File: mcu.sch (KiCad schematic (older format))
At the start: 24 parts, among them SW1 PTS645VL39-2, U4 CAT24C32, U5 STM32F765VIT6, X1 ECS-TXO-3225-160-TR

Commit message: Current snapshot
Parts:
- removed C16: 4.7uF, Capacitor_SMD:C_0603_1608Metric, symbol Device:C
- R7, R8: value 47k -> 4.7k
- renumbered C17 to C16, C22 to C17, C25 to C22, C26 to C25, C28 to C26, C30 to C28, FB1 to FB2, FB2 to FB3
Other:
- moved on the sheet: C16, C17, C22, C25, C26, C28
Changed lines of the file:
@@
 $Descr A4 11693 8268
 encoding utf-8
-Sheet 4 7
+Sheet 4 11
 Title "MCU"
 Date ""
@@
 $Comp
 L Device:C C16
-U 1 1 5AD093F4
-P 1200 7300
-F 0 "C16" H 1315 7346 50  0000 L CNN
-F 1 "4.7uF" H 1315 7255 50  0000 L CNN
-F 2 "Capacitor_SMD:C_0603_1608Metric" H 1238 7150 50  0001 C CNN
-F 3 "~" H 1200 7300 50  0001 C CNN
-	1    1200 7300
+U 1 1 5AD0945E
+P 1150 7300
+F 0 "C16" H 1265 7346 50  0000 L CNN
+F 1 "100nF" H 1265 7255 50  0000 L CNN
+F 2 "Capacitor_SMD:C_0603_1608Metric" H 1188 7150 50  0001 C CNN
+F 3 "~" H 1150 7300 50  0001 C CNN
+	1    1150 7300
 	1    0    0    -1
 $EndComp
 $Comp
 L Device:C C17
-U 1 1 5AD0945E
-P 1650 7300
-F 0 "C17" H 1765 7346 50  0000 L CNN
-F 1 "100nF" H 1765 7255 50  0000 L CNN
-F 2 "Capacitor_SMD:C_0603_1608Metric" H 1688 7150 50  0001 C CNN
-F 3 "~" H 1650 7300 50  0001 C CNN
-	1    1650 7300
+U 1 1 5AD09C8C
+P 1600 7300
+F 0 "C17" H 1715 7346 50  0000 L CNN
+F 1 "100nF" H 1715 7255 50  0000 L CNN
+F 2 "Capacitor_SMD:C_0603_1608Metric" H 1638 7150 50  0001 C CNN
+F 3 "~" H 1600 7300 50  0001 C CNN
+	1    1600 7300
 	1    0    0    -1
 $EndComp
 $Comp
 L Device:C C22
-U 1 1 5AD09C8C
-P 2100 7300
-F 0 "C22" H 2215 7346 50  0000 L CNN
-F 1 "100nF" H 2215 7255 50  0000 L CNN
-F 2 "Capacitor_SMD:C_0603_1608Metric" H 2138 7150 50  0001 C CNN
-F 3 "~" H 2100 7300 50  0001 C CNN
-	1    2100 7300
+U 1 1 5AD09D94
+P 2050 7300
+F 0 "C22" H 2165 7346 50  0000 L CNN
+F 1 "100nF" H 2165 7255 50  0000 L CNN
+F 2 "Capacitor_SMD:C_0603_1608Metric" H 2088 7150 50  0001 C CNN
+F 3 "~" H 2050 7300 50  0001 C CNN
+	1    2050 7300
 	1    0    0    -1
 $EndComp
 $Comp
 L Device:C C25
-U 1 1 5AD09D94
-P 2550 7300
-F 0 "C25" H 2665 7346 50  0000 L CNN
-F 1 "100nF" H 2665 7255 50  0000 L CNN
-F 2 "Capacitor_SMD:C_0603_1608Metric" H 2588 7150 50  0001 C CNN
-F 3 "~" H 2550 7300 50  0001 C CNN
-	1    2550 7300
+U 1 1 5AD09D9B
+P 2500 7300
+F 0 "C25" H 2615 7346 50  0000 L CNN
+F 1 "100nF" H 2615 7255 50  0000 L CNN
+F 2 "Capacitor_SMD:C_0603_1608Metric" H 2538 7150 50  0001 C CNN
+F 3 "~" H 2500 7300 50  0001 C CNN
+	1    2500 7300
 	1    0    0    -1
 $EndComp
 $Comp
 L Device:C C26
-U 1 1 5AD09D9B
-P 3000 7300
-F 0 "C26" H 3115 7346 50  0000 L CNN
-F 1 "100nF" H 3115 7255 50  0000 L CNN
-F 2 "Capacitor_SMD:C_0603_1608Metric" H 3038 7150 50  0001 C CNN
-F 3 "~" H 3000 7300 50  0001 C CNN
-	1    3000 7300
-	1    0    0    -1
-$EndComp
-$Comp
-L Device:C C28
 U 1 1 5AD09E94
-P 3450 7300
-F 0 "C28" H 3565 7346 50  0000 L CNN
-F 1 "100nF" H 3565 7255 50  0000 L CNN
-F 2 "Capacitor_SMD:C_0603_1608Metric" H 3488 7150 50  0001 C CNN
-F 3 "~" H 3450 7300 50  0001 C CNN
-	1    3450 7300
-	1    0    0    -1
-$EndComp
-Wire Wire Line
-	950  7150 1200 7150
-Connection ~ 1200 7150
-Wire Wire Line
-	1200 7150 1650 7150
-Connection ~ 1650 7150
-Wire Wire Line
-	1650 7150 2100 7150
-Connection ~ 2100 7150
-Wire Wire Line
-	2100 7150 2550 7150
-Connection ~ 2550 7150
-Wire Wire Line
-	2550 7150 3000 7150
-Connection ~ 3000 7150
-Wire Wire Line
-	3000 7150 3450 7150
-Connection ~ 1200 7450
-Wire Wire Line
-	1200 7450 950  7450
-Connection ~ 1650 7450
-Wire Wire Line
-	1650 7450 1200 7450
-Connection ~ 2100 7450
-Wire Wire Line
-	2100 7450 1650 7450
-Connection ~ 2550 7450
-Wire Wire Line
-	2550 7450 2100 7450
-Connection ~ 3000 7450
-Wire Wire Line
-	3000 7450 2550 7450
-Wire Wire Line
-	3450 7450 3000 7450
+P 2950 7300
+F 0 "C26" H 3065 7346 50  0000 L CNN
+F 1 "100nF" H 3065 7255 50  0000 L CNN
+F 2 "Capacitor_SMD:C_0603_1608Metric" H 2988 7150 50  0001 C CNN
+F 3 "~" H 2950 7300 50  0001 C CNN
+	1    2950 7300
+	1    0    0    -1
+$EndComp
 Text Notes 1650 7550 0    50   ~ 0
 Place as close as possible to pins!
@@
 $EndComp
 $Comp
-L Device:Ferrite_Bead_Small FB1
+L Device:Ferrite_Bead_Small FB2
 U 1 1 5AF6D789
 P 1250 6400
-F 0 "FB1" V 1013 6400 50  0000 C CNN
+F 0 "FB2" V 1013 6400 50  0000 C CNN
 F 1 "MPZ1608S221A" V 1104 6400 50  0000 C CNN
 F 2 "Resistor_SMD:R_0603_1608Metric" V 1180 6400 50  0001 C CNN
@@
 $EndComp
 $Comp
-L Device:Ferrite_Bead_Small FB2
+L Device:Ferrite_Bead_Small FB3
 U 1 1 5AF6DF9B
 P 1350 6500
-F 0 "FB2" V 1500 6450 50  0000 C CNN
+F 0 "FB3" V 1500 6450 50  0000 C CNN
 F 1 "MPZ1608S221A" V 1600 6450 50  0000 C CNN
 F 2 "Resistor_SMD:R_0603_1608Metric" V 1280 6500 50  0001 C CNN
@@
 VDD3V3
 $Comp
-L Device:C C30
+L Device:C C28
 U 1 1 5BC224AB
-P 3900 7300
-F 0 "C30" H 4015 7346 50  0000 L CNN
-F 1 "100nF" H 4015 7255 50  0000 L CNN
-F 2 "Capacitor_SMD:C_0603_1608Metric" H 3938 7150 50  0001 C CNN
-F 3 "~" H 3900 7300 50  0001 C CNN
-	1    3900 7300
-	1    0    0    -1
-$EndComp
-Wire Wire Line
-	3450 7150 3900 7150
-Connection ~ 3450 7150
-Wire Wire Line
-	3450 7450 3900 7450
-Connection ~ 3450 7450
+P 3400 7300
+F 0 "C28" H 3515 7346 50  0000 L CNN
+F 1 "100nF" H 3515 7255 50  0000 L CNN
+F 2 "Capacitor_SMD:C_0603_1608Metric" H 3438 7150 50  0001 C CNN
+F 3 "~" H 3400 7300 50  0001 C CNN
+	1    3400 7300
+	1    0    0    -1
+$EndComp
 Wire Wire Line
 	1300 4350 1300 4550
@@
 P 9600 5950
 F 0 "R7" H 9400 5900 50  0000 L CNN
-F 1 "47k" H 9400 6000 50  0000 L CNN
+F 1 "4.7k" H 9400 6000 50  0000 L CNN
 F 2 "Resistor_SMD:R_0603_1608Metric" V 9530 5950 50  0001 C CNN
 F 3 "~" H 9600 5950 50  0001 C CNN
@@
 P 9900 5950
 F 0 "R8" H 9700 5900 50  0000 L CNN
-F 1 "47k" H 9700 6000 50  0000 L CNN
+F 1 "4.7k" H 9700 6000 50  0000 L CNN
 F 2 "Resistor_SMD:R_0603_1608Metric" V 9830 5950 50  0001 C CNN
 F 3 "~" H 9900 5950 50  0001 C CNN
@@
 Wire Wire Line
 	7850 5100 7850 4600
+Wire Wire Line
+	950  7150 1150 7150
+Wire Wire Line
+	950  7450 1150 7450
+Connection ~ 1150 7150
+Wire Wire Line
+	1150 7150 1600 7150
+Connection ~ 1150 7450
+Wire Wire Line
+	1150 7450 1600 7450
+Connection ~ 1600 7150
+Connection ~ 1600 7450
+Connection ~ 2050 7150
+Connection ~ 2050 7450
+Connection ~ 2500 7150
+Connection ~ 2500 7450
+Connection ~ 2950 7150
+Connection ~ 2950 7450
+Wire Wire Line
+	1600 7150 2050 7150
+Wire Wire Line
+	2050 7150 2500 7150
+Wire Wire Line
+	2500 7150 2950 7150
+Wire Wire Line
+	2950 7150 3400 7150
+Wire Wire Line
+	2050 7450 2500 7450
+Wire Wire Line
+	2500 7450 2950 7450
+Wire Wire Line
+	2950 7450 3400 7450
+Wire Wire Line
+	1600 7450 2050 7450
 $EndSCHEMATC

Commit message: First pass of routing
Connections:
- net SCL: now also U5.92 (PB6)
- net SDA: now also U5.96 (PB9)
- net Z_MIN: now reaches U5.1 (PE2)
- net TEMP4: now reaches U5.15 (PC0)
- net TEMP3: now reaches U5.16 (PC1)
- net TEMP2: now reaches U5.17 (PC2)
- net TEMP1: now reaches U5.18 (PC3)
- net Y_MIN: now reaches U5.2 (PE3)
- net PWM_HEAT1: now reaches U5.22 (PA0-WKUP)
- net STEP_Z: now reaches U5.23 (PA1)
- net STEP_Y: now reaches U5.24 (PA2)
- net STEP_X: now reaches U5.25 (PA3)
- net MCU_SS: now reaches U5.28 (PA4)
- net SPI1_SCK: now reaches U5.29 (PA5)
- net X_MIN: now reaches U5.3 (PE4)
- net SPI1_MISO: now reaches U5.30 (PA6)
- net SPI1_MOSI: now reaches U5.31 (PA7)
- net DIR_Z: now reaches U5.33 (PC5)
- net SS_Z: now reaches U5.34 (PB0)
- net DIR_Y: now reaches U5.35 (PB1)
- net SS_Y: now reaches U5.36 (PB2)
- net DIR_X: now reaches U5.37 (PE7)
- net SS_X: now reaches U5.38 (PE8)
- net PWM_BED: now reaches U5.4 (PE5)
- net SPI4_SCK: now reaches U5.42 (PE12)
- net SPI4_MISO: now reaches U5.43 (PE13)
- net SPI4_MOSI: now reaches U5.44 (PE14)
- net DIR_E1: now reaches U5.46 (PB10)
- net PWM_HEAT2: now reaches U5.5 (PE6)
- net SS_E1: now reaches U5.51 (PB12)
- net DIR_E0: now reaches U5.52 (PB13)
- net STEP_E1: now reaches U5.53 (PB14)
- net STEP_E0: now reaches U5.54 (PB15)
- net SS_E0: now reaches U5.56 (PD9)
- net SS_SD: now reaches U5.57 (PD10)
- net SD_DETECT: now reaches U5.58 (PD11)
- net PWM_FAN1: now reaches U5.59 (PD12)
- net PWM_FAN2: now reaches U5.60 (PD13)
- net PWM_FAN3: now reaches U5.61 (PD14)
- net PWM_FAN4: now reaches U5.62 (PD15)
- net PWM_EXT4: now reaches U5.63 (PC6)
- net PWM_EXT3: now reaches U5.64 (PC7)
- net PWM_EXT2: now reaches U5.65 (PC8)
- net PWM_EXT1: now reaches U5.66 (PC9)
- net USART1_TX: now reaches U5.68 (PA9)
- net USART1_RX: now reaches U5.69 (PA10)
- net SWDIO: now reaches U5.72 (PA13)
- net SWCLK: now reaches U5.76 (PA14)
- net USART3_TX: now reaches U5.78 (PC10)
- net USART3_RX: now reaches U5.79 (PC11)
- net D5: now reaches U5.83 (PD2)
- net D4: now reaches U5.84 (PD3)
- net D3: now reaches U5.85 (PD4)
- net D2: now reaches U5.86 (PD5)
- net D1: now reaches U5.87 (PD6)
- net SWO: now reaches U5.89 (PB3)
- no-connect marks 3 -> 25
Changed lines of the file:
@@
 	0    1    1    0
-$EndComp
-$Comp
-L heteromycin:STM32F765VIT6 U5
-U 1 1 5AD0AB9A
-P 6750 3000
-F 0 "U5" H 6750 3000 50  0000 L CNN
-F 1 "STM32F765VIT6" H 6500 2900 50  0000 L CNN
-F 2 "heteromycin:TQFP-100_14x14mm_P0.5mm" H 6750 3000 50  0001 C CNN
-F 3 "http://www.st.com/en/microcontrollers/stm32f765vi.html" H 6750 3000 50  0001 C CNN
-	1    6750 3000
-	1    0    0    -1
 $EndComp
 Text HLabel 10400 6200 2    50   Input ~ 0
@@
 Wire Wire Line
 	1600 7450 2050 7450
+Text HLabel 5150 2100 0    50   Input ~ 0
+PWM_BED
+Text HLabel 5150 2200 0    50   Input ~ 0
+PWM_HEAT2
+Text HLabel 5150 3500 0    50   Input ~ 0
+TEMP1
+Text HLabel 5150 3400 0    50   Input ~ 0
+TEMP2
+Text HLabel 5150 3300 0    50   Input ~ 0
+TEMP3
+Text HLabel 5150 3200 0    50   Input ~ 0
+TEMP4
+Text HLabel 5150 3900 0    50   Input ~ 0
+PWM_HEAT1
+Text HLabel 5150 4000 0    50   Input ~ 0
+STEP_Z
+Text HLabel 5150 4100 0    50   Input ~ 0
+STEP_Y
+Text HLabel 5150 4200 0    50   Input ~ 0
+STEP_X
+Text HLabel 5850 4600 3    50   Input ~ 0
+SPI1_SCK
+Text HLabel 5950 4600 3    50   Input ~ 0
+SPI1_MISO
+Text HLabel 6050 4600 3    50   Input ~ 0
+SPI1_MOSI
+NoConn ~ 6150 4600
+NoConn ~ 6850 4600
+NoConn ~ 6950 4600
+Text HLabel 6350 4600 3    50   Input ~ 0
+SS_Z
+Text HLabel 6250 4600 3    50   Input ~ 0
+DIR_Z
+Text HLabel 6550 4600 3    50   Input ~ 0
+SS_Y
+Text HLabel 6450 4600 3    50   Input ~ 0
+DIR_Y
+Text HLabel 6750 4600 3    50   Input ~ 0
+SS_X
+Text HLabel 5750 4600 3    50   Input ~ 0
+MCU_SS
+Text HLabel 7150 4600 3    50   Input ~ 0
+SPI4_SCK
+Text HLabel 7250 4600 3    50   Input ~ 0
+SPI4_MISO
+NoConn ~ 7450 4600
+Text HLabel 7350 4600 3    50   Input ~ 0
+SPI4_MOSI
+Text HLabel 7550 4600 3    50   Input ~ 0
+DIR_E1
+Text HLabel 8350 4200 2    50   Input ~ 0
+SS_E1
+Text HLabel 8350 4100 2    50   Input ~ 0
+DIR_E0
+Text HLabel 8350 3700 2    50   Input ~ 0
+SS_E0
+Text HLabel 8350 4000 2    50   Input ~ 0
+STEP_E1
+Text HLabel 8350 3900 2    50   Input ~ 0
+STEP_E0
+Text HLabel 8350 3400 2    50   Input ~ 0
+PWM_FAN1
+Text HLabel 8350 3300 2    50   Input ~ 0
+PWM_FAN2
+Text HLabel 8350 3200 2    50   Input ~ 0
+PWM_FAN3
+Text HLabel 8350 3100 2    50   Input ~ 0
+PWM_FAN4
+Text HLabel 8350 2700 2    50   Input ~ 0
+PWM_EXT1
+Text HLabel 8350 2800 2    50   Input ~ 0
+PWM_EXT2
+Text HLabel 8350 2900 2    50   Input ~ 0
+PWM_EXT3
+Text HLabel 8350 3000 2    50   Input ~ 0
+PWM_EXT4
+Text HLabel 8350 2500 2    50   Input ~ 0
+USART1_TX
+Text HLabel 8350 2400 2    50   Input ~ 0
+USART1_RX
+NoConn ~ 8350 2300
+Text HLabel 8350 3600 2    50   Input ~ 0
+SS_SD
+NoConn ~ 8350 2600
+NoConn ~ 8350 2200
+Text HLabel 8350 2100 2    50   Input ~ 0
+SWDIO
+Text HLabel 7950 1400 1    50   Input ~ 0
+SWCLK
+Text HLabel 6650 1400 1    50   Input ~ 0
+SWO
+Text HLabel 7750 1400 1    50   Input ~ 0
+USART3_TX
+Text HLabel 7650 1400 1    50   Input ~ 0
+USART3_RX
+Text HLabel 6350 1400 1    50   Input ~ 0
+SCL
+Text HLabel 5950 1400 1    50   Input ~ 0
+SDA
+NoConn ~ 5150 2400
+NoConn ~ 7850 1400
+NoConn ~ 7550 1400
+NoConn ~ 7450 1400
+NoConn ~ 6750 1400
+NoConn ~ 6550 1400
+NoConn ~ 6450 1400
+NoConn ~ 6250 1400
+NoConn ~ 6050 1400
+NoConn ~ 5850 1400
+NoConn ~ 5750 1400
+Text HLabel 6650 4600 3    50   Input ~ 0
+DIR_X
+NoConn ~ 8350 3800
+NoConn ~ 7650 4600
+Text HLabel 8350 3500 2    50   Input ~ 0
+SD_DETECT
+NoConn ~ 7050 4600
+Text HLabel 5150 2000 0    50   Input ~ 0
+X_MIN
+Text HLabel 5150 1900 0    50   Input ~ 0
+Y_MIN
+Text HLabel 5150 1800 0    50   Input ~ 0
+Z_MIN
+$Comp
+L heteromycin:STM32F765VIT6 U5
+U 1 1 5AD0AB9A
+P 6750 3000
+F 0 "U5" H 6750 3000 50  0000 L CNN
+F 1 "STM32F765VIT6" H 6500 2900 50  0000 L CNN
+F 2 "heteromycin:TQFP-100_14x14mm_P0.5mm" H 6750 3000 50  0001 C CNN
+F 3 "http://www.st.com/en/microcontrollers/stm32f765vi.html" H 6750 3000 50  0001 C CNN
+	1    6750 3000
+	1    0    0    -1
+$EndComp
+Text HLabel 6850 1400 1    50   Input ~ 0
+D1
+Text HLabel 6950 1400 1    50   Input ~ 0
+D2
+Text HLabel 7050 1400 1    50   Input ~ 0
+D3
+Text HLabel 7150 1400 1    50   Input ~ 0
+D4
+Text HLabel 7250 1400 1    50   Input ~ 0
+D5
+NoConn ~ 7350 1400
 $EndSCHEMATC

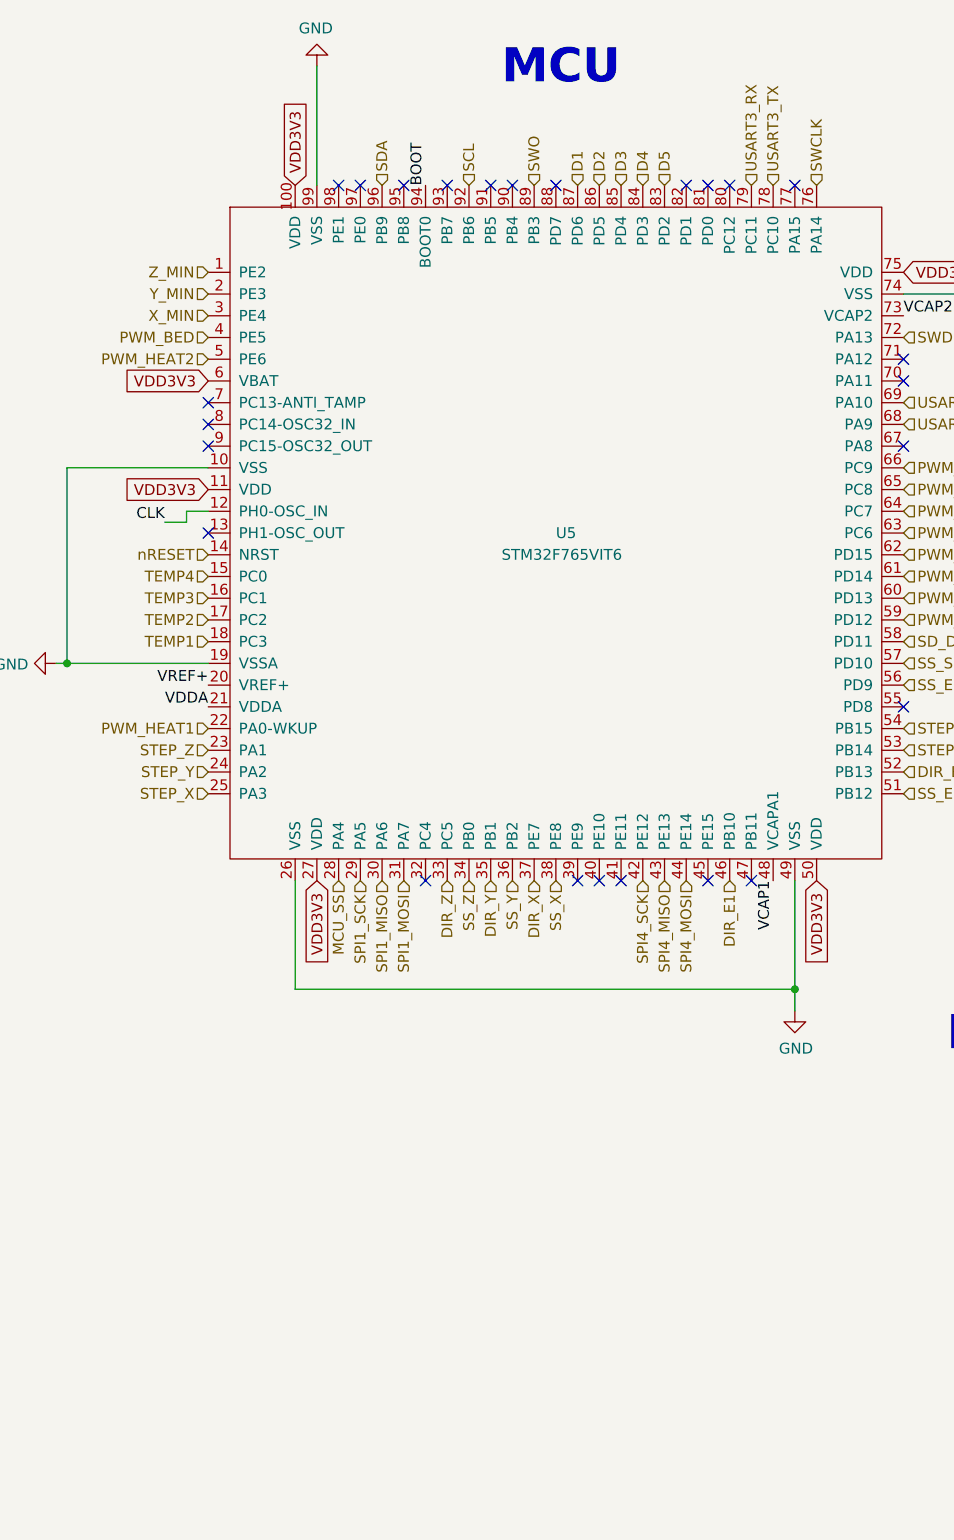
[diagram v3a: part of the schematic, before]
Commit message: Various changes
* Add Status LED
* Switched small diodes to more general available BAT54 in SOD123
* Fixed various DRC errors
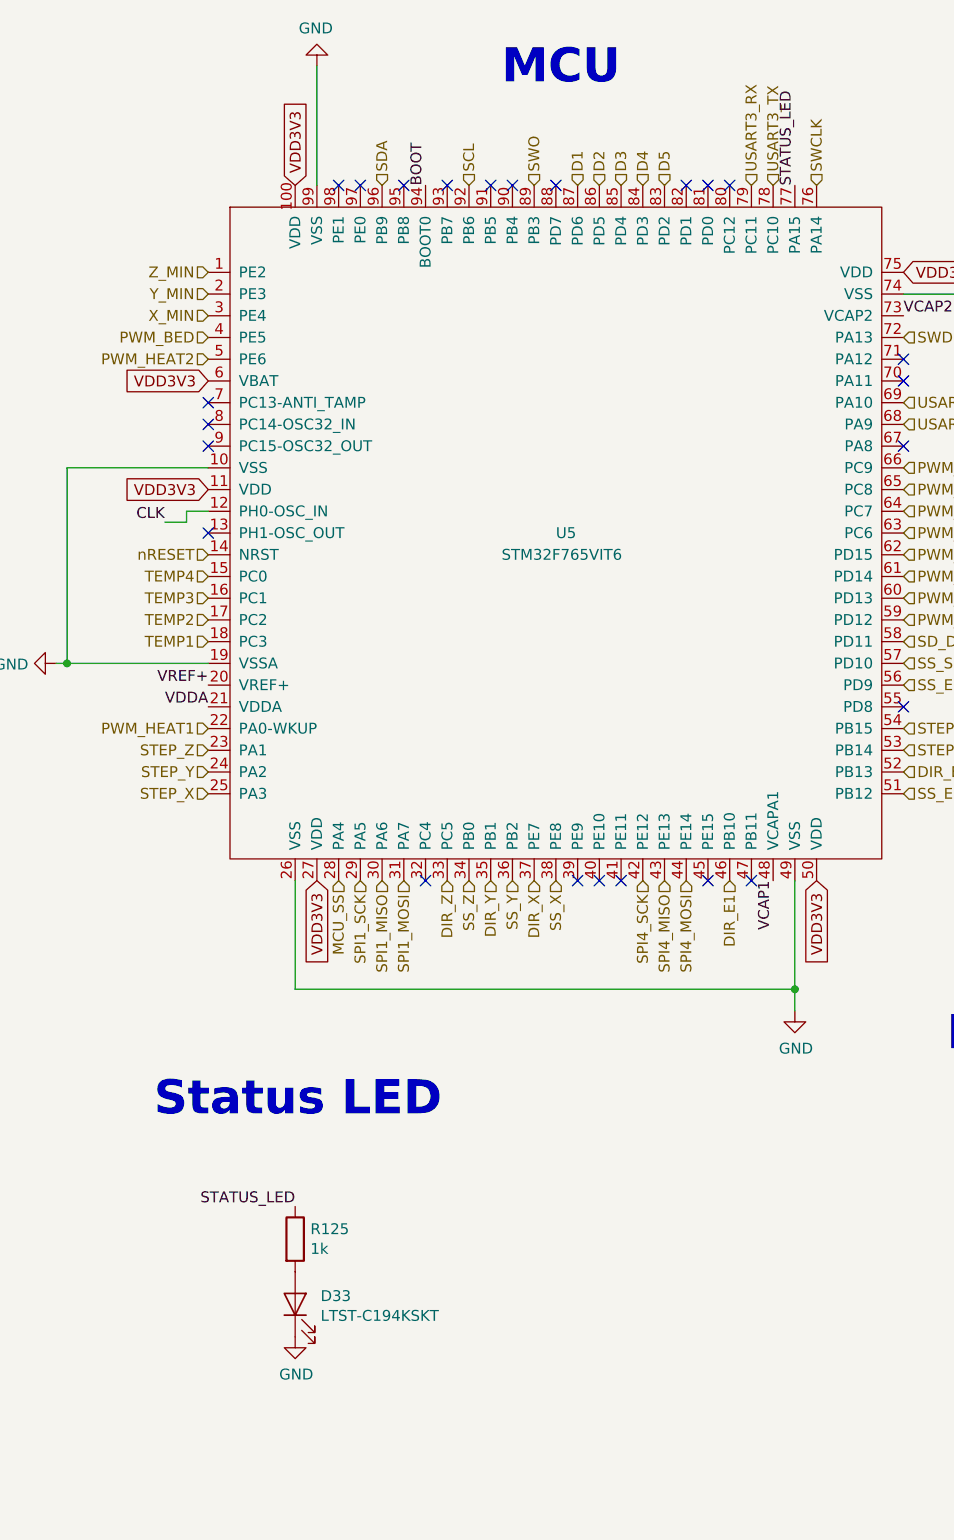
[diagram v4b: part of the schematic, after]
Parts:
- added D33: LTST-C194KSKT, LED_SMD:LED_0603_1608Metric, symbol Device:LED
- added R125: 1k, Resistor_SMD:R_0603_1608Metric, symbol Device:R
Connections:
- net GND: now also D33.1 (K)
- net STATUS_LED: now reaches U5.77 (PA15)
- net STATUS_LED: now also R125.1
- new net: D33.2 (A), R125.2
- no-connect marks 25 -> 24
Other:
- note added: "Status LED"
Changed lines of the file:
@@
 SDA
 NoConn ~ 5150 2400
-NoConn ~ 7850 1400
 NoConn ~ 7550 1400
 NoConn ~ 7450 1400
@@
 D5
 NoConn ~ 7350 1400
+Text Label 7850 1400 1    50   ~ 0
+STATUS_LED
+Text Label 5550 6100 2    50   ~ 0
+STATUS_LED
+Text Notes 4900 5700 0    157  ~ 31
+Status LED
+$Comp
+L Device:R R?
+U 1 1 5BCE7FB5
+P 5550 6250
+AR Path="/5BC54251/5BCE7FB5" Ref="R?"  Part="1"
+AR Path="/5BC1C8A4/5BCE7FB5" Ref="R125"  Part="1"
+F 0 "R125" H 5620 6296 50  0000 L CNN
+F 1 "1k" H 5620 6205 50  0000 L CNN
+F 2 "Resistor_SMD:R_0603_1608Metric" V 5480 6250 50  0001 C CNN
+F 3 "~" H 5550 6250 50  0001 C CNN
+	1    5550 6250
+	1    0    0    -1
+$EndComp
+$Comp
+L Device:LED D?
+U 1 1 5BCE7FBC
+P 5550 6550
+AR Path="/5BC54251/5BCE7FBC" Ref="D?"  Part="1"
+AR Path="/5BC1C8A4/5BCE7FBC" Ref="D33"  Part="1"
+F 0 "D33" V 5588 6433 50  0000 R CNN
+F 1 "LTST-C194KSKT" V 5497 6433 50  0000 R CNN
+F 2 "LED_SMD:LED_0603_1608Metric" H 5550 6550 50  0001 C CNN
+F 3 "~" H 5550 6550 50  0001 C CNN
+	1    5550 6550
+	0    -1   -1   0
+$EndComp
+$Comp
+L power:GND #PWR0131
+U 1 1 5BCEB458
+P 5550 6700
+F 0 "#PWR0131" H 5550 6450 50  0001 C CNN
+F 1 "GND" H 5555 6527 50  0000 C CNN
+F 2 "" H 5550 6700 50  0001 C CNN
+F 3 "" H 5550 6700 50  0001 C CNN
+	1    5550 6700
+	1    0    0    -1
+$EndComp
 $EndSCHEMATC

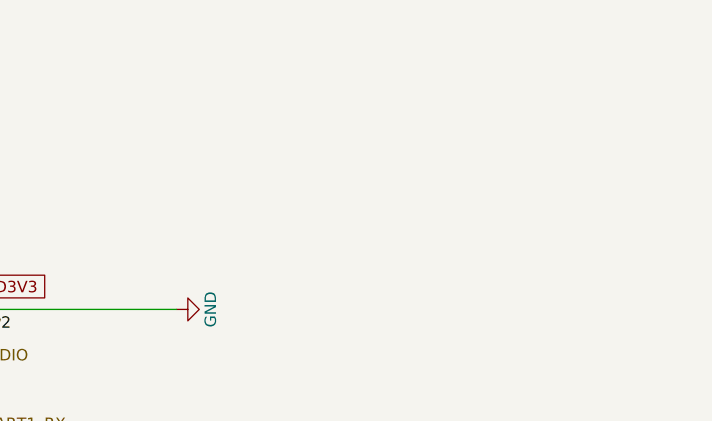
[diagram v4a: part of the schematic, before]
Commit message: Add i3a component
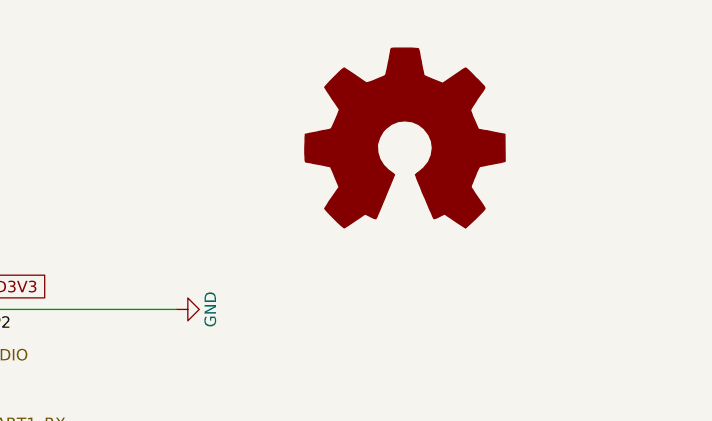
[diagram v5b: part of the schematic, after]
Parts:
- added LOGO1: Logo_Open_Hardware_Large, Symbol:OSHW-Logo2_14.6x12mm_SilkScreen, symbol Graphic:Logo_Open_Hardware_Large
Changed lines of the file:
@@
+	1    0    0    -1
+$EndComp
+$Comp
+L Graphic:Logo_Open_Hardware_Large LOGO1
+U 1 1 5BD3A860
+P 10300 1200
+F 0 "LOGO1" H 10300 1700 50  0001 C CNN
+F 1 "Logo_Open_Hardware_Large" H 10300 800 50  0001 C CNN
+F 2 "Symbol:OSHW-Logo2_14.6x12mm_SilkScreen" H 10300 1200 50  0001 C CNN
+F 3 "~" H 10300 1200 50  0001 C CNN
+	1    10300 1200
 	1    0    0    -1
 $EndComp
